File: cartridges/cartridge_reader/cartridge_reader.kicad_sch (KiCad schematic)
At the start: 3 parts

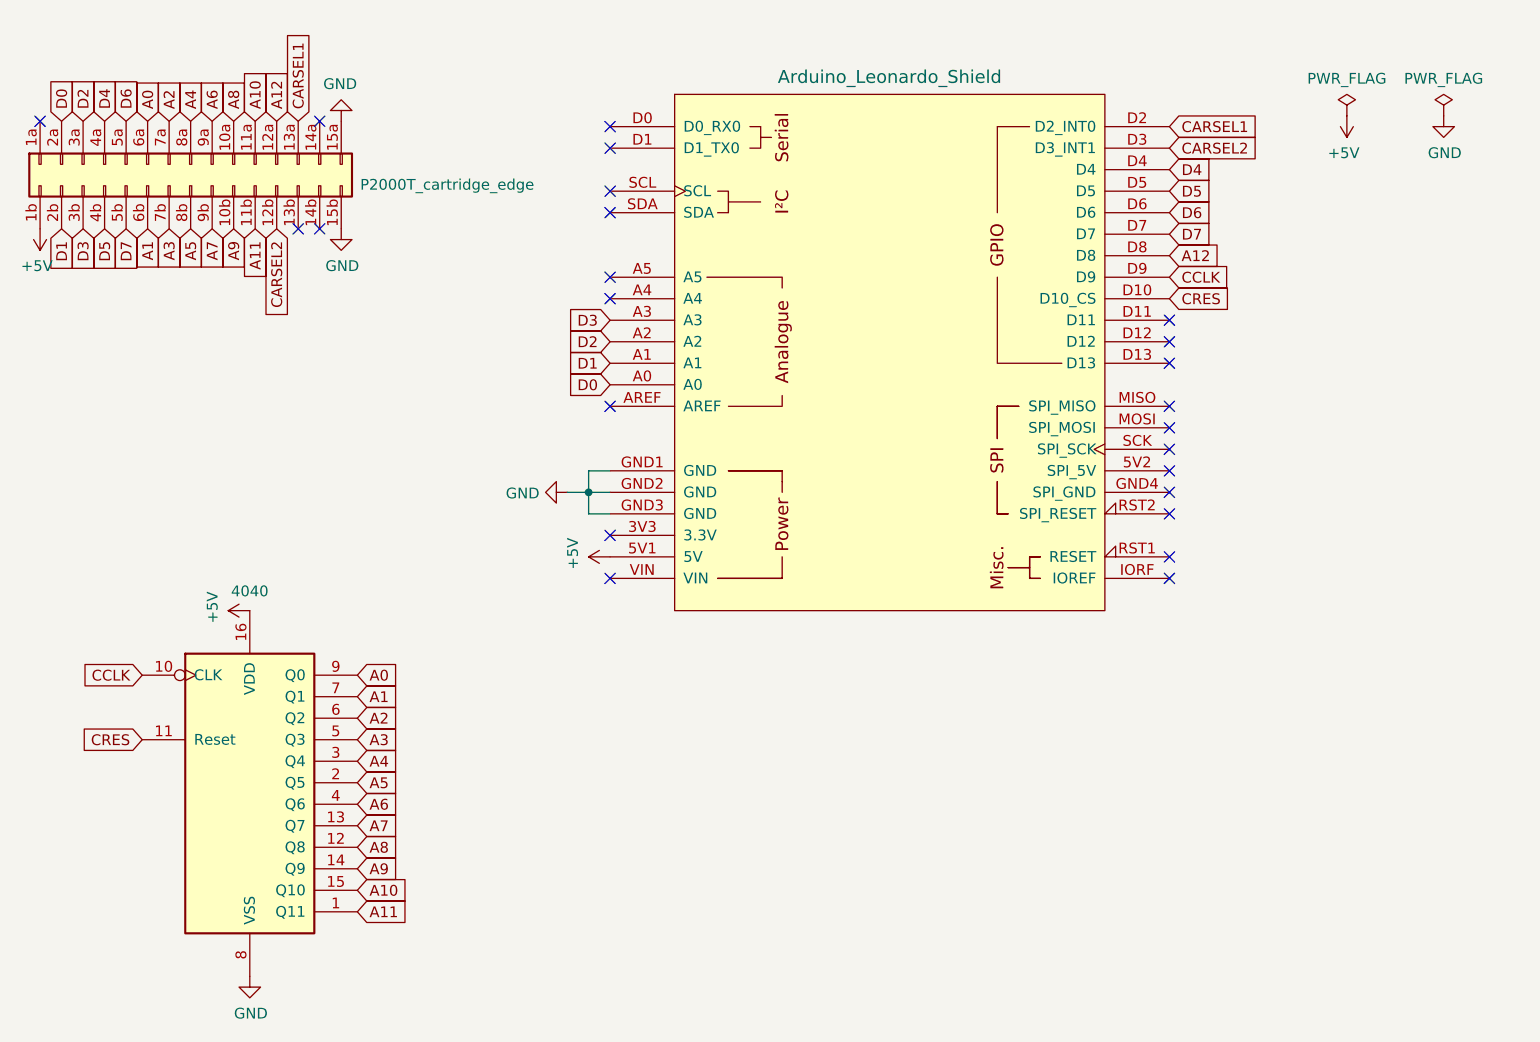
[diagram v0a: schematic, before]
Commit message: Making small adjustments to lay-out
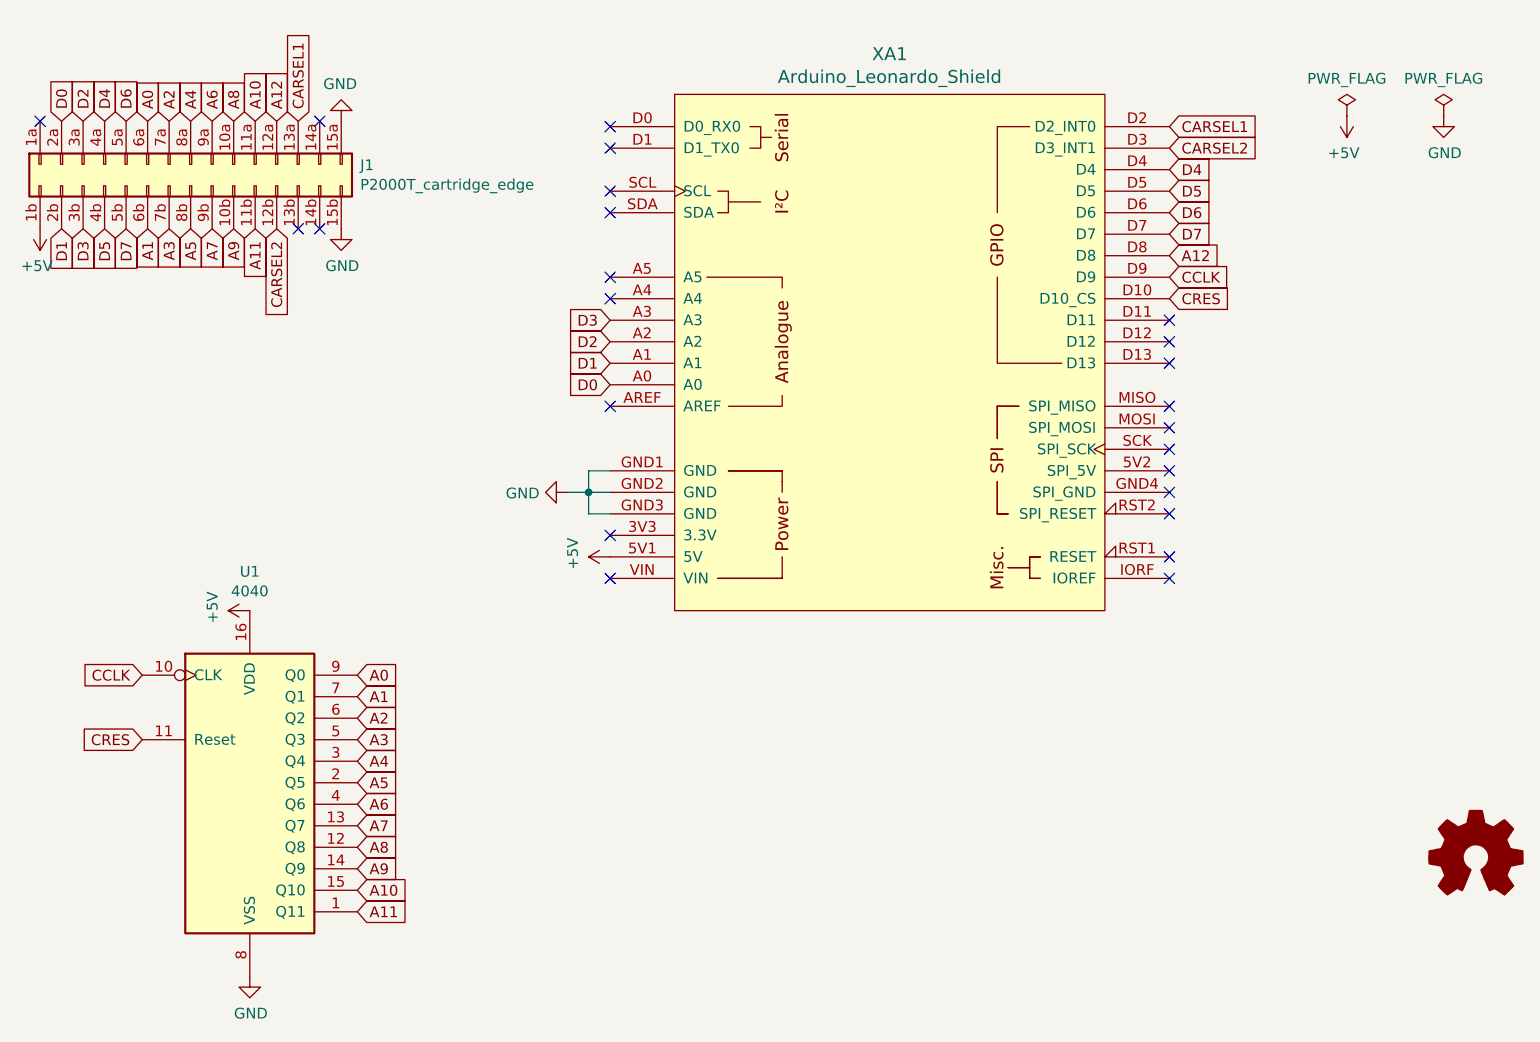
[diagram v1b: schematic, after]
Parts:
- gave numbers to parts that had none: 3
